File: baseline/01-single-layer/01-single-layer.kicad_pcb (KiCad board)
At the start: 2 copper layers, 52.1 x 46.4 mm, 15 parts, among them P1 IN, P2 OUT, P3 POWER, P4 CONN_2, P5 MOUNTING_HOLE, P6 MOUNTING_HOLE, P7 MOUNTING_HOLE, P8 MOUNTING_HOLE, U1 ECC83

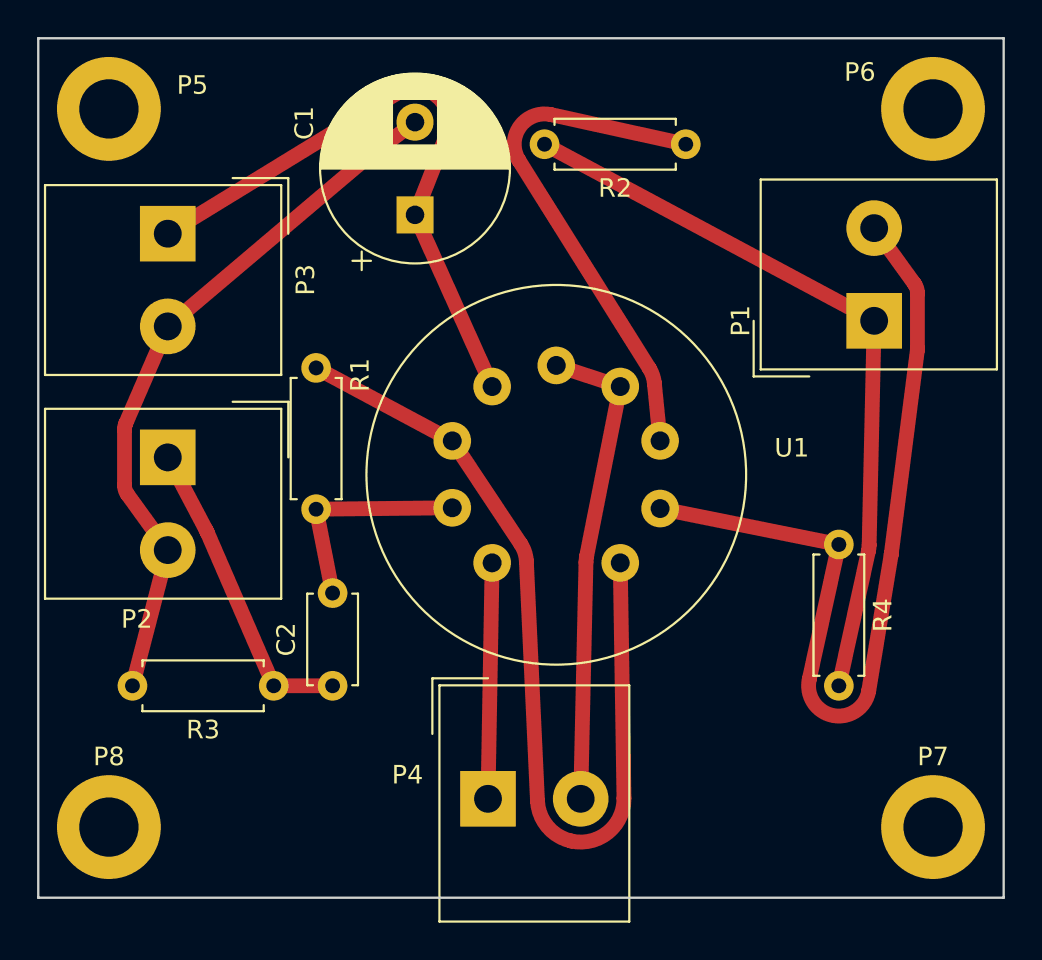
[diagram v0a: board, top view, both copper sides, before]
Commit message: feat(bundle): route nets as a seated bundle rather than one after another
Sequential routing has a failure no ordering can fix. A gap wide enough
for two tracks: the first net through it is asked, alone, where a rubber
band would sit, and a rubber band sits in the middle. The second finds
the gap full. Re-routing the first puts it back exactly where it was --
the taut path is deterministic -- so ripping up and re-ordering only
swaps who is stranded.

Routing now happens in two stages. Every connection is first routed
against the static obstacles alone, which says which gap it *wants* --
including connections that a sequential pass would have blocked, so a
stranded net still gets a say. Gaps are then counted,
floor((D - c) / (w + c)) tracks each, contending nets are ordered across
each gap and given slots, and every connection is routed again against
obstacles inflated by its own slot's share. Nothing is pushed: each net
is simply handed a problem that already contains the others.

The slack in a gap has to be divided rather than handed to every net.
Giving each the full band let them all drift to the inside of it and end
up 1.5 apart where 2.0 was required; folding an equal share into the
stride fixes it, and any position in one band is then a full pitch from
any position in the next.

Slot assignment is a model, so the arrangement is verified afterwards on
real geometry and anything still too close is routed the old way. That
settling pass also reconsiders which layer a connection sits on --
choosing it before the contention is known left a two-layer board using
one layer and stranding a net on it.

Results are unchanged on all three boards, and that is the honest
finding rather than a disappointment to hide:

  ecc83-pp F.Cu        19/20 -> 19/20
  ecc83-pp F.Cu+B.Cu   20/20 -> 20/20
  sonde xilinx         63/66 -> 63/66, 0 DRC either way

The mechanism is proven on the case it exists for -- tests/test_bundle.py
shows the second net raising NoPathFound sequentiall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
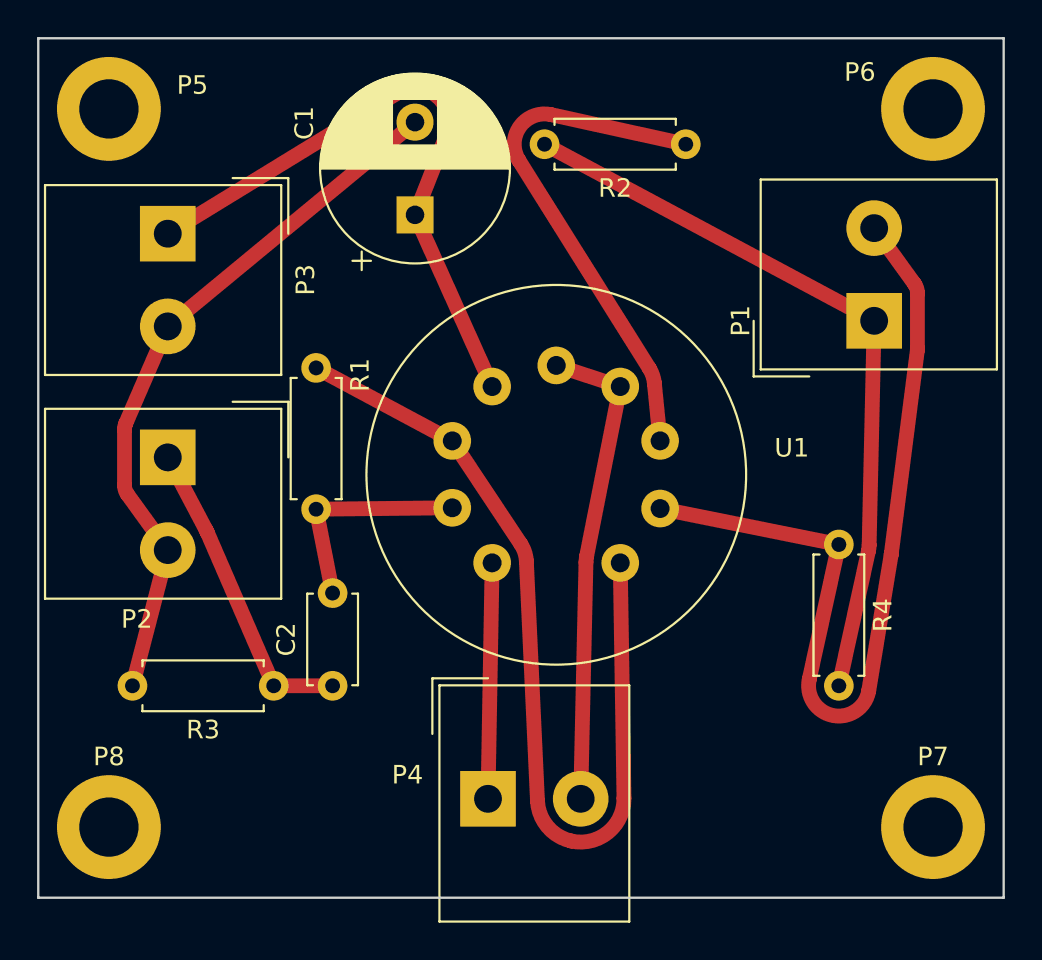
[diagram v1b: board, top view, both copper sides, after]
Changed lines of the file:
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@@
 	(segment
 		(start 141.605 94.695)
-		(end 139.046033 96.591777)
-		(width 0.8)
-		(layer "F.Cu")
-		(net 1)
-	)
-	(segment
-		(start 139.046033 96.591777)
-		(end 138.913032 96.697209)
-		(width 0.8)
-		(layer "F.Cu")
-		(net 1)
-	)
-	(segment
-		(start 138.913032 96.697209)
 		(end 128.27 105.711)
 		(width 0.8)
@@
 	(segment
 		(start 166.077241 125.360774)
-		(end 167.286071 118.02775)
+		(end 167.286071 118.027751)
 		(width 0.8)
 		(layer "F.Cu")
@@
 	)
 	(segment
-		(start 167.286071 118.02775)
-		(end 167.292505 117.983805)
+		(start 167.286071 118.027751)
+		(end 167.292506 117.983805)
 		(width 0.8)
 		(layer "F.Cu")
@@
 	)
 	(segment
-		(start 167.292505 117.983805)
+		(start 167.292506 117.983805)
 		(end 168.697243 107.015951)
 		(width 0.8)
